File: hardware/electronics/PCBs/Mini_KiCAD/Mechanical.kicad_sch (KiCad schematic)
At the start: 32 parts

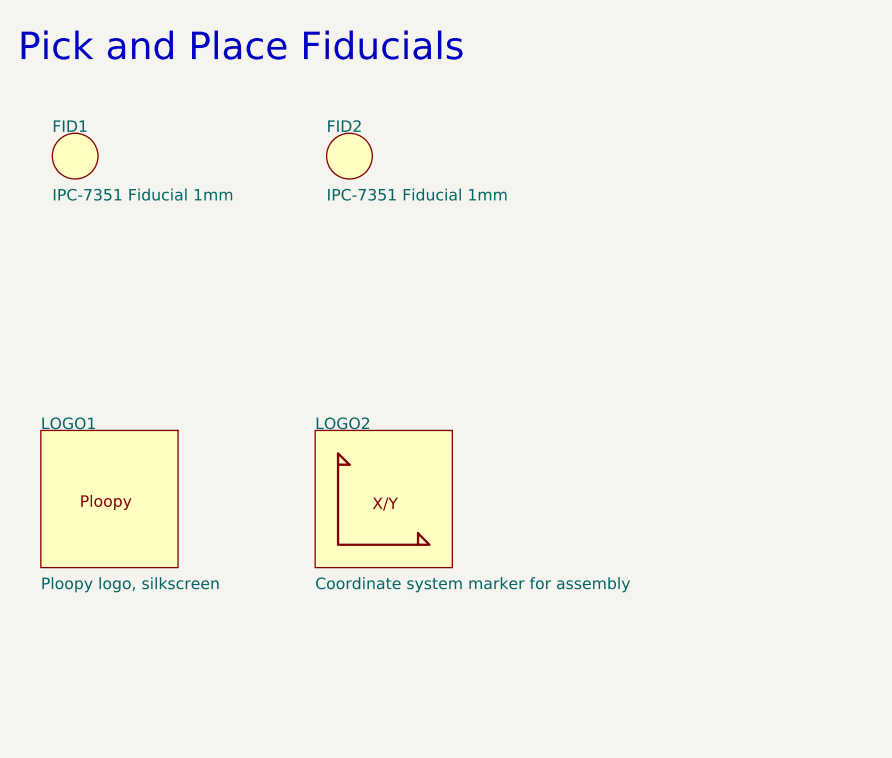
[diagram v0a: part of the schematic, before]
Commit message: Initial commit of the PCB project file replacing the ADNS-5050 with PMW3360, referencing the schematic of the Ploopy Classic.
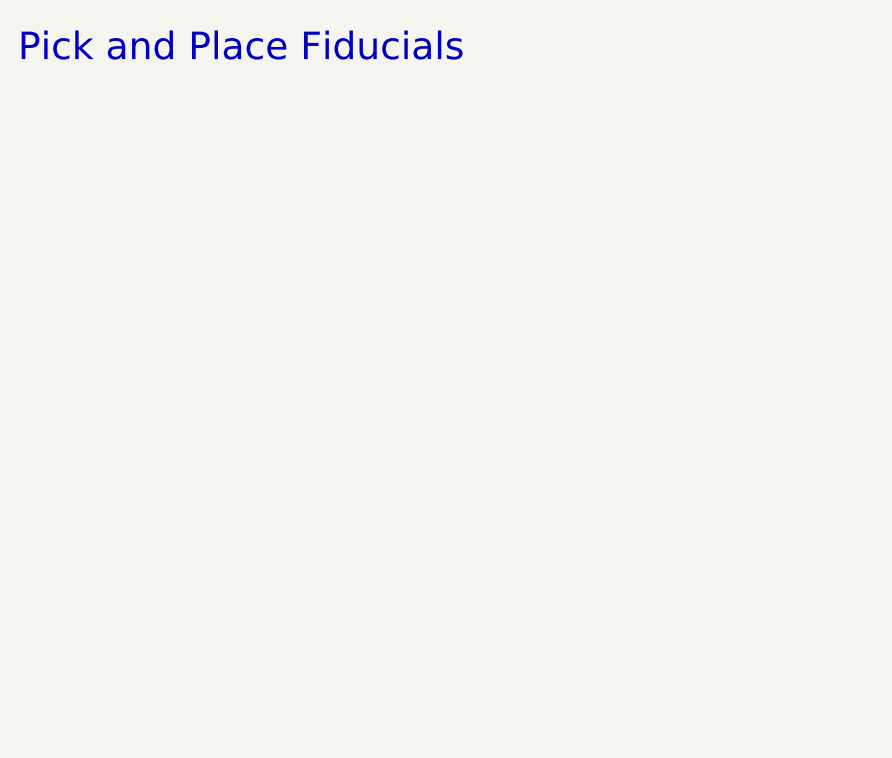
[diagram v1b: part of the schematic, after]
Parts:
- removed FID1: IPC-7351 Fiducial 1mm, symbol Mini-altium-import:MCH_0_FIDUCIAL_1.5
- removed FID2: IPC-7351 Fiducial 1mm, FIDUCIAL_1.5, symbol Mini-altium-import:MCH_0_FIDUCIAL_1.5
- removed LOGO1: Ploopy logo, silkscreen, PloopyLogo, symbol Mini-altium-import:MCH_0_PloopyLogo
- removed LOGO2: Coordinate system marker for assembly, Coordinate System, symbol Mini-altium-import:MCH_0_CoordinateSystem
- MCH.SP.1, MCH.SP.10, MCH.SP.11, MCH.SP.12, MCH.SP.13, MCH.SP.14, MCH.SP.15, MCH.SP.16, MCH.SP.17, MCH.SP.18, MCH.SP.19, MCH.SP.2, MCH.SP.20, MCH.SP.21, MCH.SP.22, MCH.SP.23, MCH.SP.24, MCH.SP.25, MCH.SP.26, MCH.SP.27, MCH.SP.28, MCH.SP.3, MCH.SP.4, MCH.SP.5, MCH.SP.6, MCH.SP.7, MCH.SP.8, MCH.SP.9: footprint SparkGap -> PCBFeatures.PcbLib:SparkGap
